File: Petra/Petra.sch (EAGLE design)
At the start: 26 parts, among them J2 AVR_SPI_PRG_6NS, J3 Side, J4 Bottom, J5 Top, U1 MIC5219 5V, Y1 16MHz

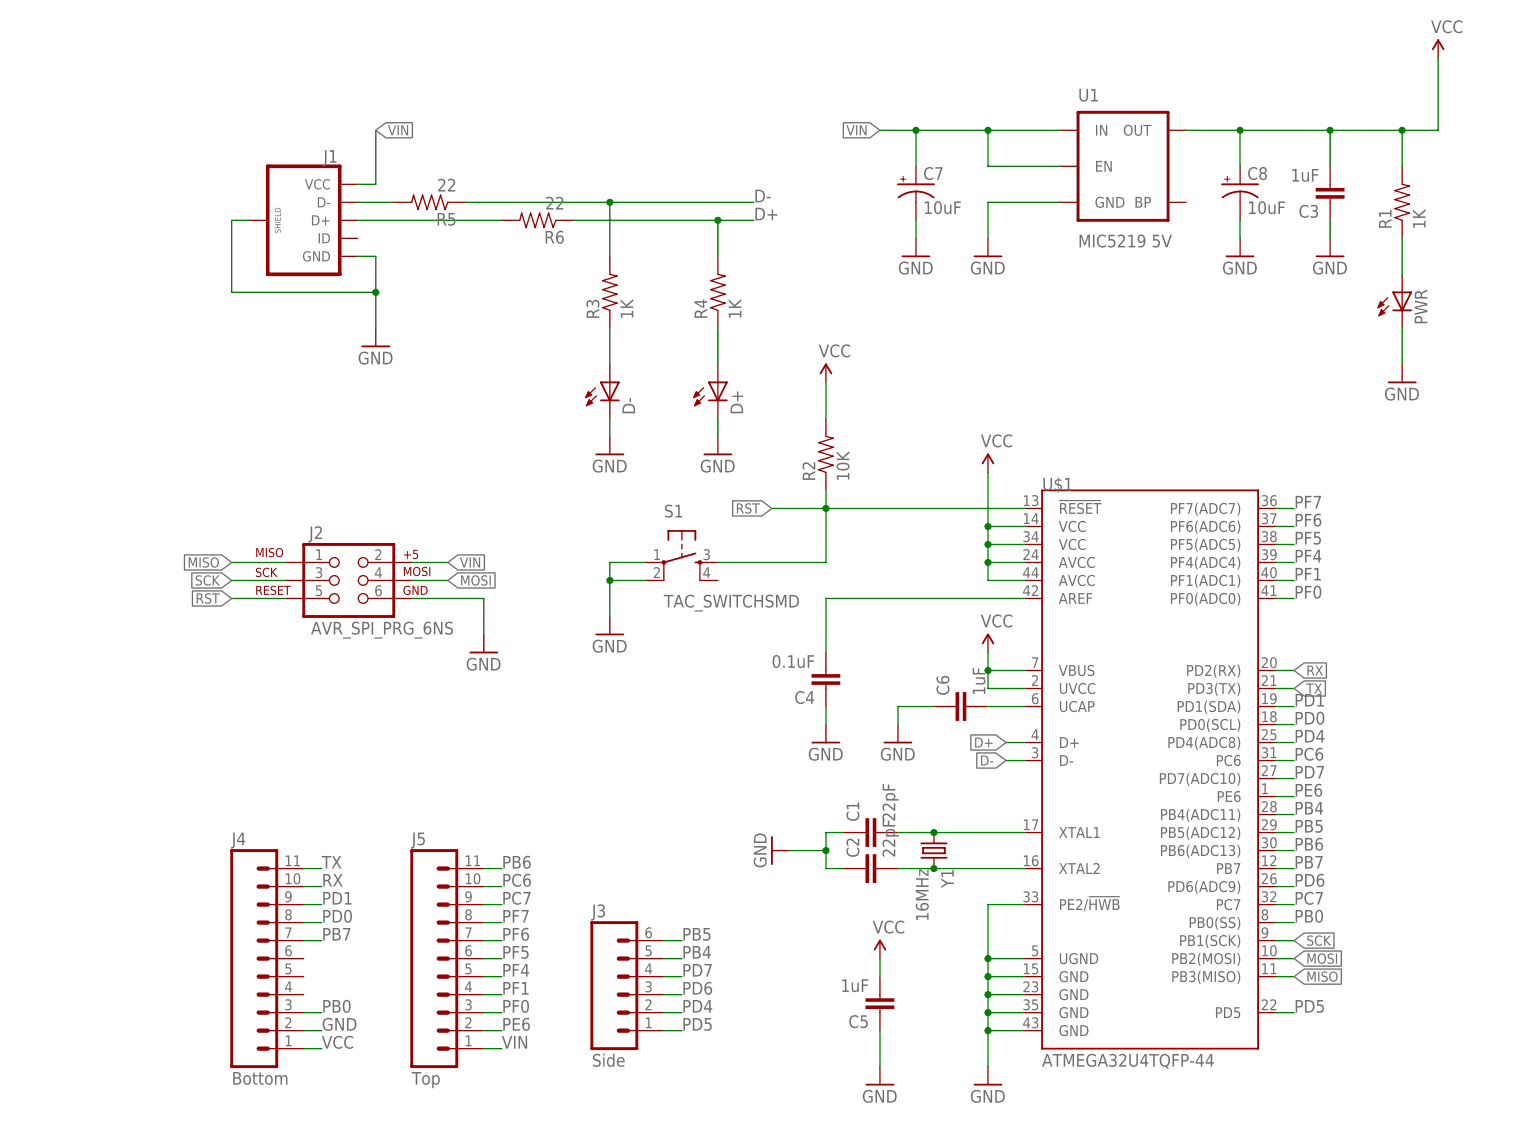
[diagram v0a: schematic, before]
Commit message: Created Screw Terminal Board. Cleaned up folder structure.
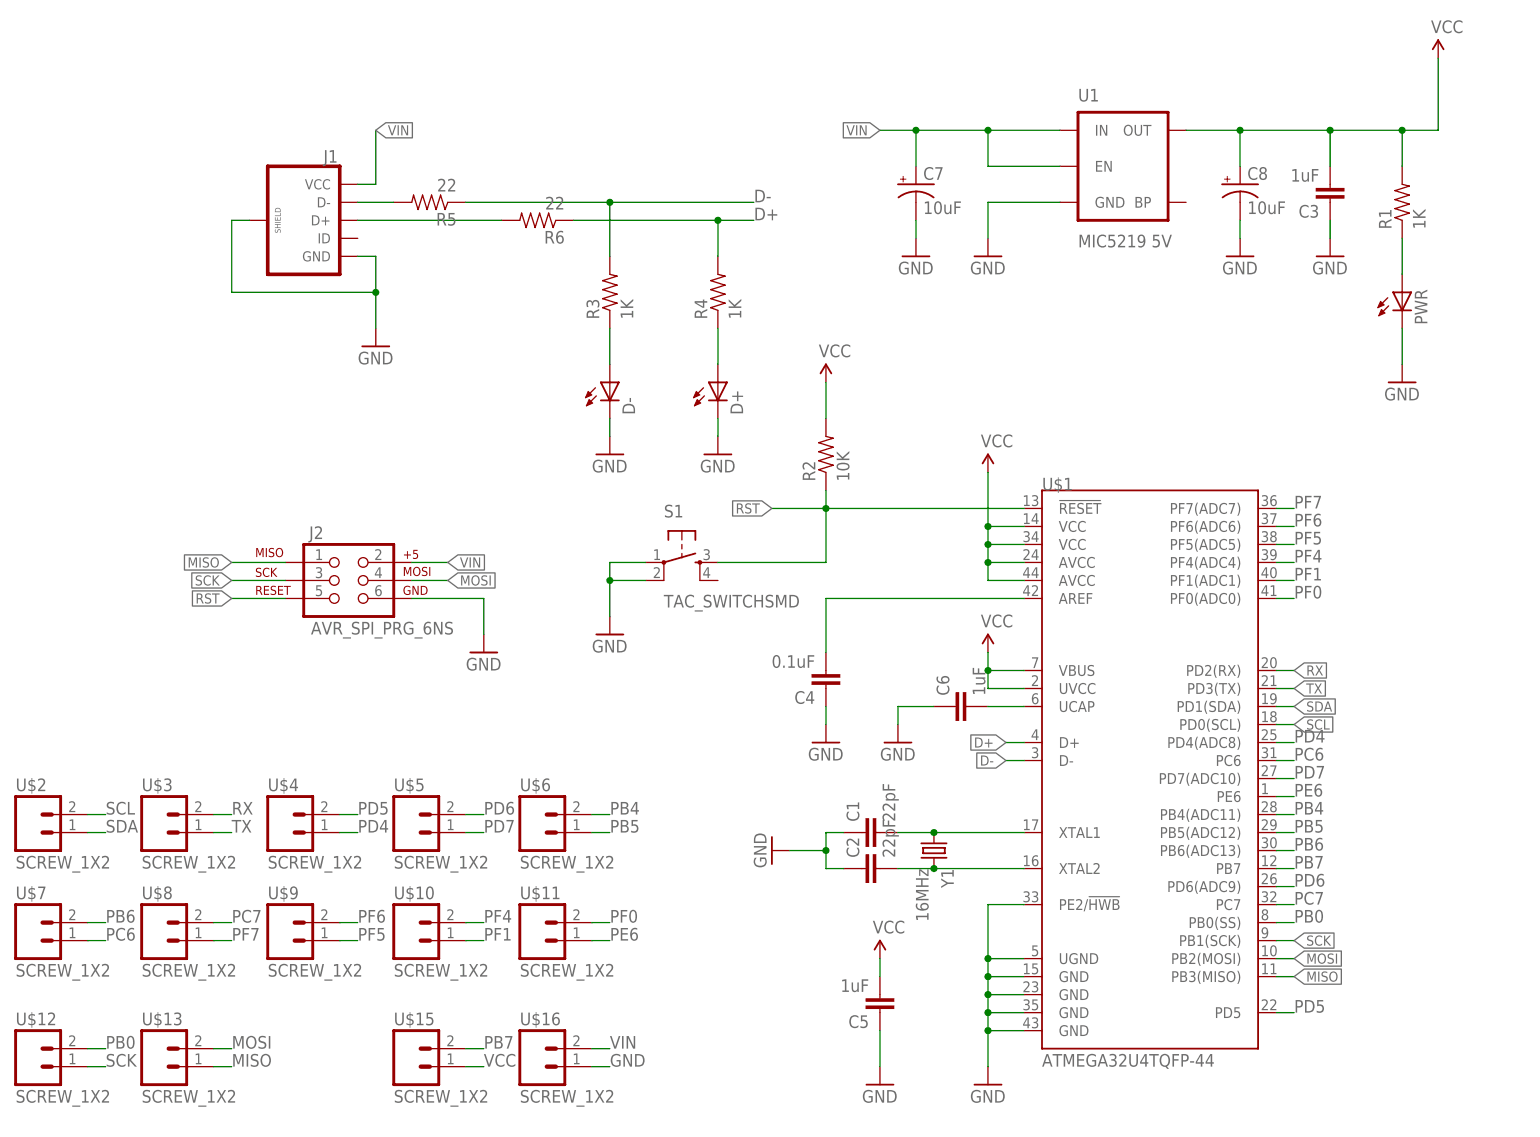
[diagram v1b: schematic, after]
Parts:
- removed J3: Side, SparkFun-Connectors:M06POGOPIN_HOLES_ONLY
- removed J4: Bottom, SparkFun-Connectors:M11POGOPIN_HOLES_ONLY
- removed J5: Top, SparkFun-Connectors:M11POGOPIN_HOLES_ONLY
- added U$10, U$11, U$12, U$13, U$15, U$16, U$2, U$3, U$4, U$5, U$6, U$7, U$8, U$9: SCREW_1X2, PartsYouNeed:SCREW_1X2
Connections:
- removed net PD0: J4.8, U$1.PD0(SCL)
- removed net PD1: J4.9, U$1.PD1(SDA)
- new net SCL: U$1.PD0(SCL), U$2.2
- new net SDA: U$1.PD1(SDA), U$2.1
- net GND: now also U$16.1; no longer J4.2
- net MISO: now also U$13.1
- net MOSI: now also U$13.2
- net PB0: now also U$12.2; no longer J4.3
- net PB4: now also U$6.2; no longer J3.5
- net PB5: now also U$6.1; no longer J3.6
- net PB6: now also U$7.2; no longer J5.11
- net PB7: now also U$15.2; no longer J4.7
- net PC6: now also U$7.1; no longer J5.10
- net PC7: now also U$8.2; no longer J5.9
- net PD4: now also U$4.1; no longer J3.2
- net PD5: now also U$4.2; no longer J3.1
- net PD6: now also U$5.2; no longer J3.3
- net PD7: now also U$5.1; no longer J3.4
- net PE6: now also U$11.1; no longer J5.2
- net PF0: now also U$11.2; no longer J5.3
- net PF1: now also U$10.1; no longer J5.4
- net PF4: now also U$10.2; no longer J5.5
- net PF5: now also U$9.1; no longer J5.6
- net PF6: now also U$9.2; no longer J5.7
- net PF7: now also U$8.1; no longer J5.8
- net RX: now also U$3.2; no longer J4.10
- net SCK: now also U$12.1
- net TX: now also U$3.1; no longer J4.11
- net VCC: now also U$15.1; no longer J4.1
- net VIN: now also U$16.2; no longer J5.1

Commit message: Made screw terminal board smaller. Added BOM for Petra
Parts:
- added C9: 1uF, SparkFun-Passives:CAP0402-CAP
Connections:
- net GND: now also C9.1
- net VCC: now also C9.2
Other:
- moved on the sheet: U$10, U$11, U$12, U$13, U$15, U$16, U$2, U$3, U$4, U$5, U$6, U$7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

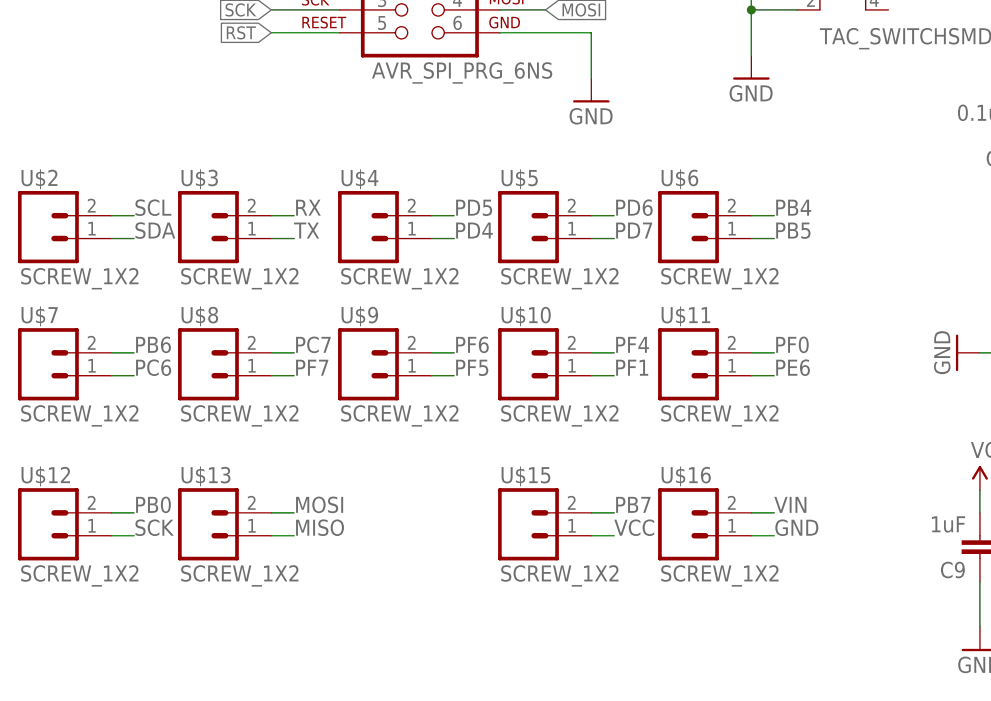
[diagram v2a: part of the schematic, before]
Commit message: moving to 20 pin io connector
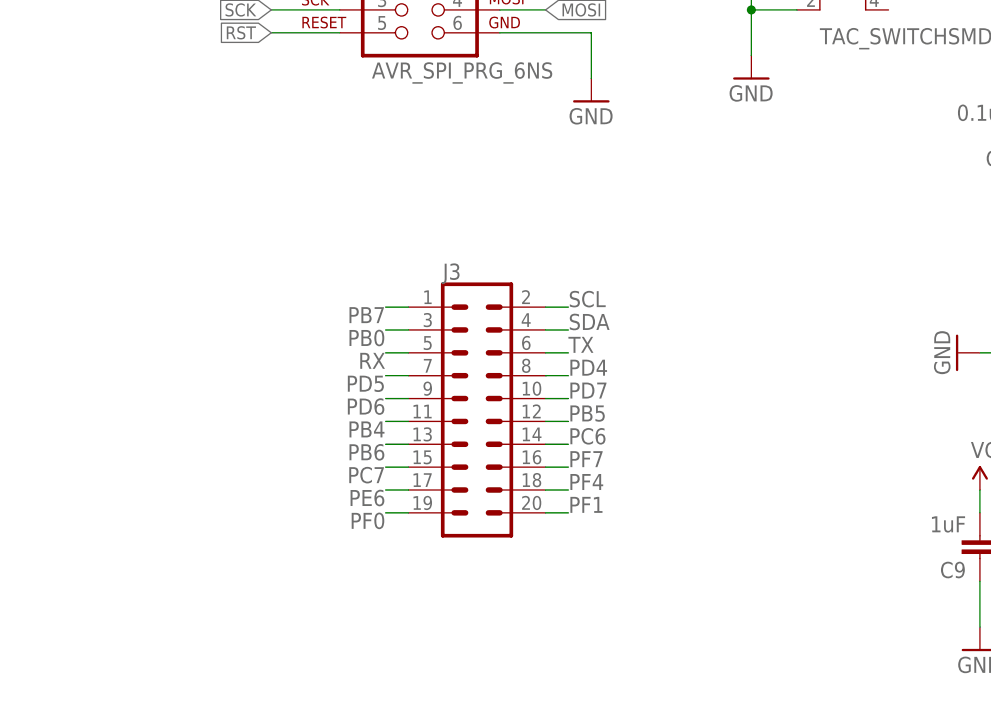
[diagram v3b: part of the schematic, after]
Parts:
- removed U$10, U$11, U$12, U$13, U$15, U$16, U$2, U$3, U$4, U$5, U$6, U$7, U$8, U$9: SCREW_1X2, PartsYouNeed:SCREW_1X2
- added J3: (no value), SparkFun-Connectors:CONN_10X2
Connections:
- net GND: no longer U$16.1
- net MISO: no longer U$13.1
- net MOSI: no longer U$13.2
- net PB0: now also J3.3; no longer U$12.2
- net PB4: now also J3.11; no longer U$6.2
- net PB5: now also J3.12; no longer U$6.1
- net PB6: now also J3.13; no longer U$7.2
- net PB7: now also J3.1; no longer U$15.2
- net PC6: now also J3.14; no longer U$7.1
- net PC7: now also J3.15; no longer U$8.2
- net PD4: now also J3.8; no longer U$4.1
- net PD5: now also J3.7; no longer U$4.2
- net PD6: now also J3.9; no longer U$5.2
- net PD7: now also J3.10; no longer U$5.1
- net PE6: now also J3.17; no longer U$11.1
- net PF0: now also J3.19; no longer U$11.2
- net PF1: now also J3.20; no longer U$10.1
- net PF4: now also J3.18; no longer U$10.2
- net PF5: no longer U$9.1
- net PF6: no longer U$9.2
- net PF7: now also J3.16; no longer U$8.1
- net RX: now also J3.5; no longer U$3.2
- net SCK: no longer U$12.1
- net SCL: now also J3.2; no longer U$2.2
- net SDA: now also J3.4; no longer U$2.1
- net TX: now also J3.6; no longer U$3.1
- net VCC: no longer U$15.1
- net VIN: no longer U$16.2

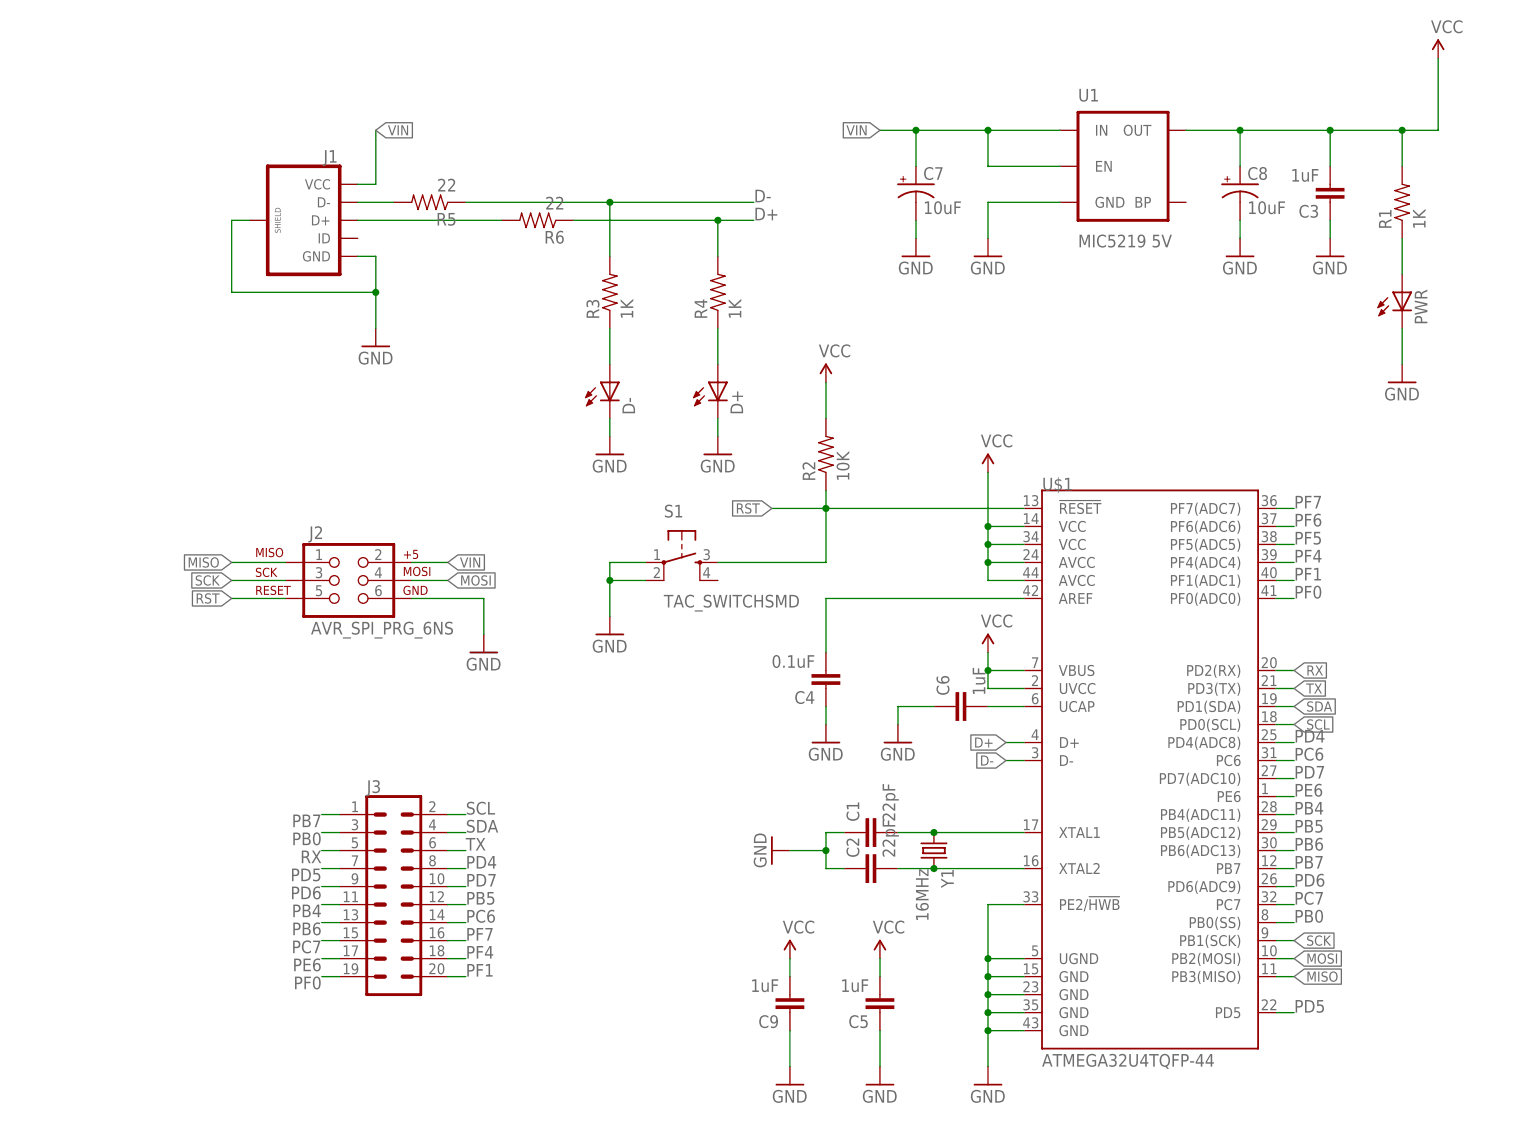
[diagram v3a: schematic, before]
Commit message: Completed io change. Reduced board size
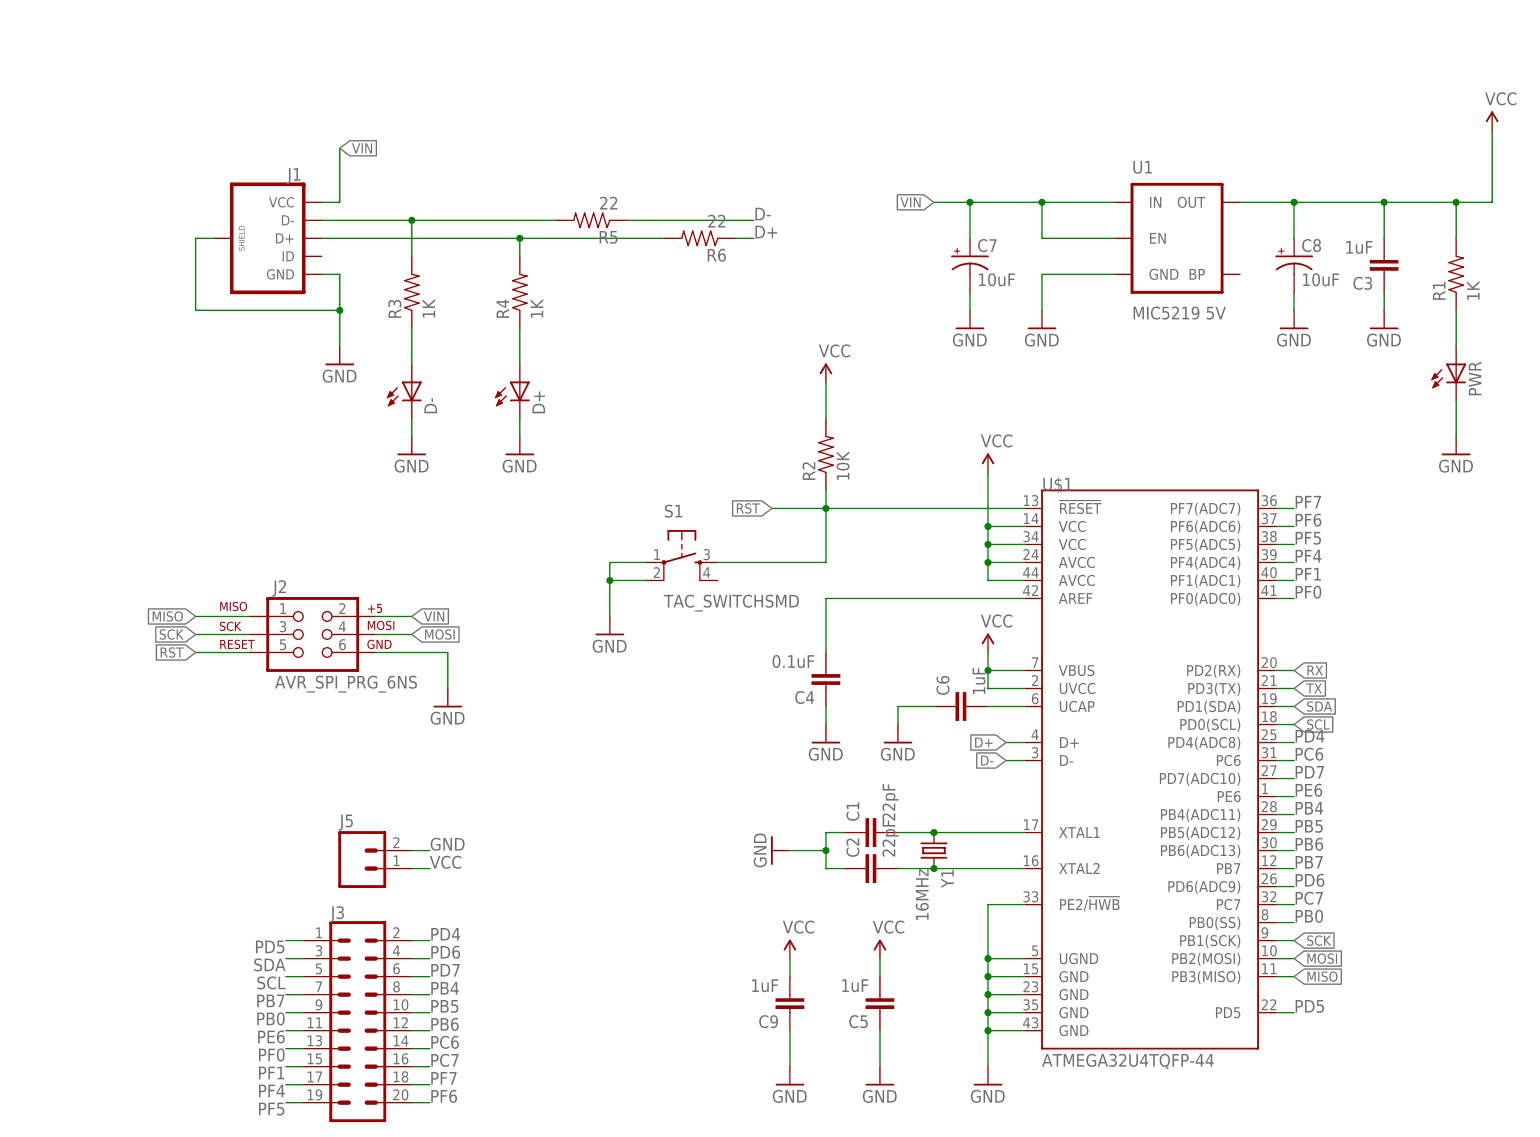
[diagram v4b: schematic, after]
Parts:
- added J5: (no value), SparkFun-Connectors:M02PTH
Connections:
- net D+: no longer R4.2
- net D-: no longer R3.2
- net GND: now also J5.2
- net N$5: now also R3.2
- net N$6: now also R4.2
- net PB0: now also J3.9; no longer J3.3
- net PB4: now also J3.8; no longer J3.11
- net PB5: now also J3.10; no longer J3.12
- net PB6: now also J3.12; no longer J3.13
- net PB7: now also J3.7; no longer J3.1
- net PC7: now also J3.16; no longer J3.15
- net PD4: now also J3.2; no longer J3.8
- net PD5: now also J3.1; no longer J3.7
- net PD6: now also J3.4; no longer J3.9
- net PD7: now also J3.6; no longer J3.10
- net PE6: now also J3.11; no longer J3.17
- net PF0: now also J3.13; no longer J3.19
- net PF1: now also J3.15; no longer J3.20
- net PF4: now also J3.17; no longer J3.18
- net PF5: now also J3.19
- net PF6: now also J3.20
- net PF7: now also J3.18; no longer J3.16
- net RX: no longer J3.5
- net SCL: now also J3.5; no longer J3.2
- net SDA: now also J3.3; no longer J3.4
- net TX: no longer J3.6
- net VCC: now also J5.1
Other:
- moved on the sheet: C3, C7, C8, D+, D-, J1, J2, J3, PWR, R1, R3, R4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
